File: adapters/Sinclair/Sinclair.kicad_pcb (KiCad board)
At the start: 2 copper layers, 22.9 x 18.4 mm, 2 parts, among them J1 JoyKEY, J2 Sinclair

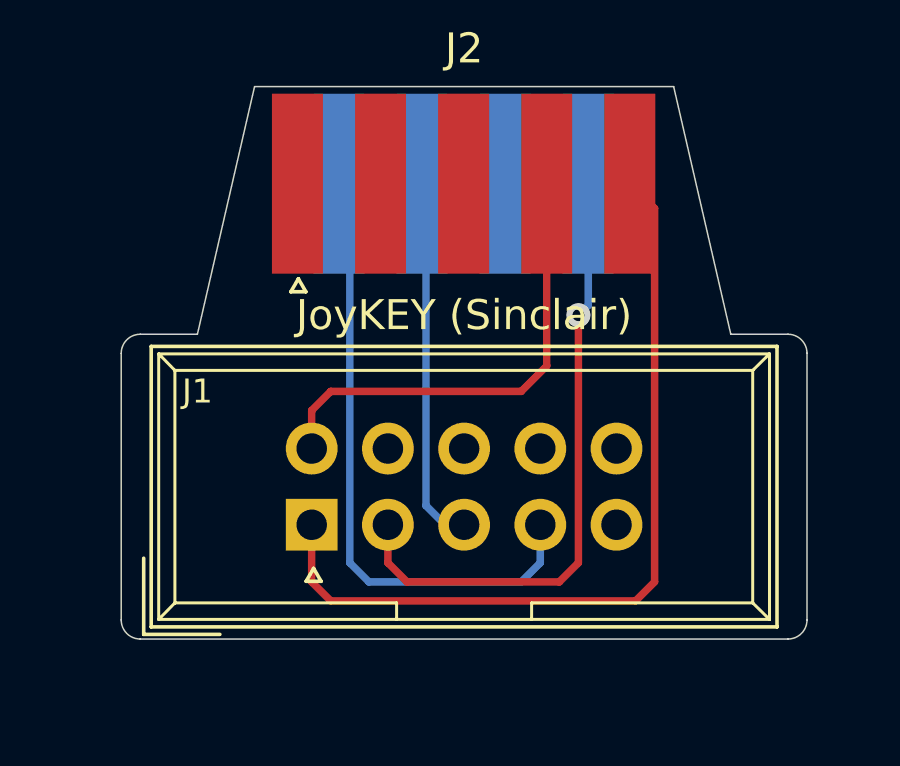
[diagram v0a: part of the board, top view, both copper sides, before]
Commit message: Fixed Sinclair adapter
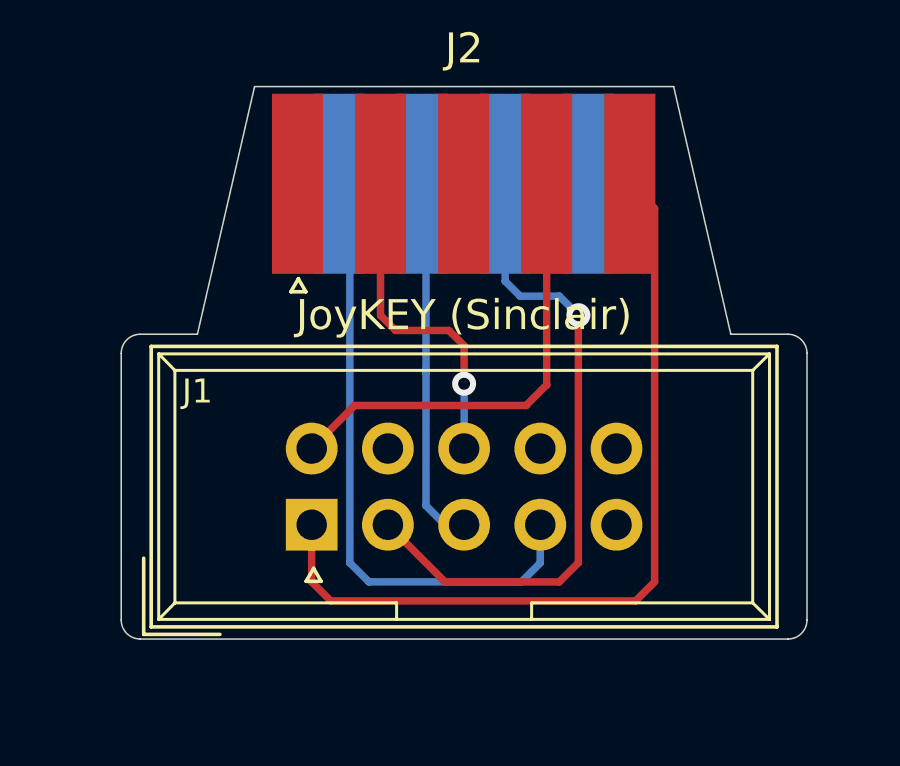
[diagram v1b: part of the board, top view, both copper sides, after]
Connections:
- J1 pad 10: Net-(J1-Pad10) -> (no net)
- J1 pad 5: Net-(J1-Pad5) -> (no net)
- J1 pad 7: Net-(J1-Pad7) -> (no net)
- J1 pad 9: Net-(J1-Pad9) -> (no net)
- J2 pad 1: Net-(J2-Pad1) -> (no net)
- J2 pad 2: Net-(J2-Pad2) -> GND
- J2 pad 3: Net-(J2-Pad3) -> (no net)
- J2 pad 8: GND -> /DOWN
- J2 pad 9: /DOWN -> (no net)
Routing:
- net GND: track 0.00 -> 11.0 mm, vias 0 -> 1
- net /DOWN: track 20.9 -> 21.8 mm

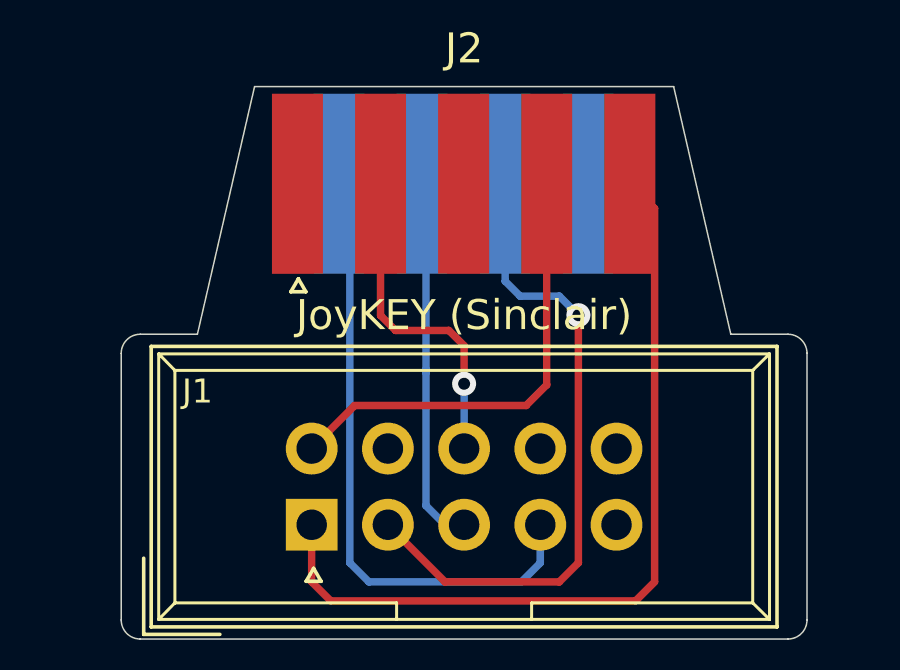
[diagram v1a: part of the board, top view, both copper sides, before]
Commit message: Tweaked sinclair adapter
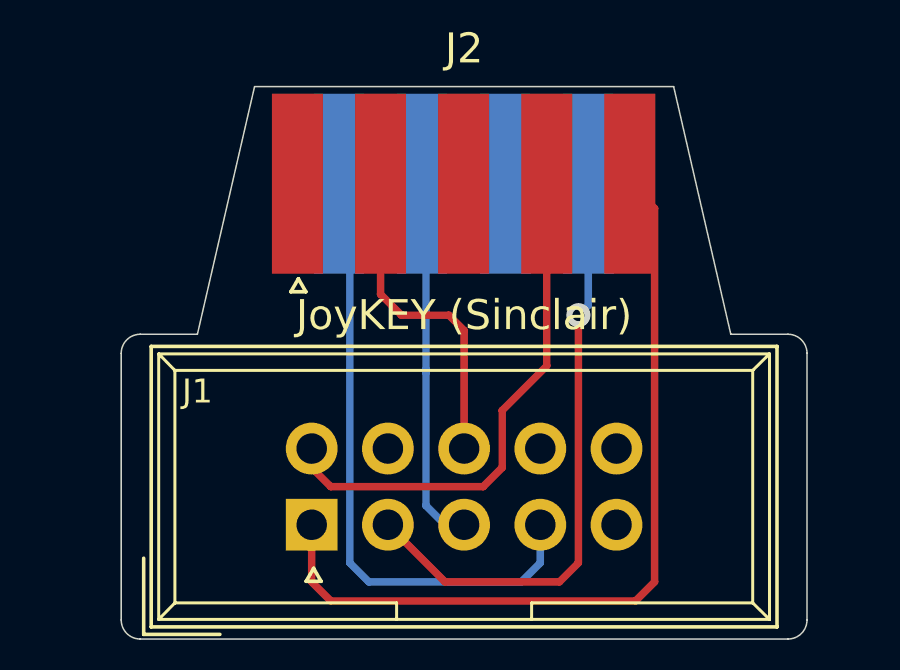
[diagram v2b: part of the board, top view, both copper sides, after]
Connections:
- J2 pad 8: /DOWN -> GND
- J2 pad 9: (no net) -> /DOWN
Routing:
- net /FIRE: track 15.4 -> 17.6 mm
- net /DOWN: track 21.8 -> 20.2 mm
- net GND: track 11.0 -> 10.9 mm, vias 1 -> 0
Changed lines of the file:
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@@
     (thickness 1.6)
     (drawings 16)
-    (tracks 38)
+    (tracks 37)
     (zones 0)
     (modules 2)
@@
       (net 4 /LEFT))
     (pad 8 smd rect (at 1.3695 0.0635 180) (size 1.7 6) (layers B.Cu B.Paste B.Mask)
+      (net 1 GND))
+    (pad 9 smd rect (at 4.1395 0.0635 180) (size 1.7 6) (layers B.Cu B.Paste B.Mask)
       (net 3 /DOWN))
-    (pad 9 smd rect (at 4.1395 0.0635 180) (size 1.7 6) (layers B.Cu B.Paste B.Mask))
     (pad 1 smd rect (at -5.5555 0.0635 180) (size 1.7 6) (layers F.Cu F.Paste F.Mask))
     (pad 2 smd rect (at -2.7855 0.0635 180) (size 1.7 6) (layers F.Cu F.Paste F.Mask)
@@
   (gr_line (start 130.81 92.71) (end 130.81 83.82) (layer Edge.Cuts) (width 0.05))
   (gr_line (start 153.035 93.345) (end 131.445 93.345) (layer Edge.Cuts) (width 0.05))
-  (via (at 142.24 84.836) (size 0.8) (drill 0.4) (layers F.Cu B.Cu) (net 1))
-  (segment (start 142.24 86.995) (end 142.24 84.836) (width 0.25) (layer B.Cu) (net 1))
-  (segment (start 142.24 83.566) (end 142.24 84.836) (width 0.25) (layer F.Cu) (net 1))
-  (segment (start 141.732 83.058) (end 142.24 83.566) (width 0.25) (layer F.Cu) (net 1))
-  (segment (start 139.954 83.058) (end 141.732 83.058) (width 0.25) (layer F.Cu) (net 1))
-  (segment (start 139.4545 82.5585) (end 139.954 83.058) (width 0.25) (layer F.Cu) (net 1))
-  (segment (start 139.4545 78.1685) (end 139.4545 82.5585) (width 0.25) (layer F.Cu) (net 1))
+  (segment (start 139.4545 78.1685) (end 139.4545 81.854185) (width 0.25) (layer F.Cu) (net 1) (status 10))
+  (segment (start 139.4545 81.854185) (end 140.150315 82.55) (width 0.25) (layer F.Cu) (net 1))
+  (segment (start 140.150315 82.55) (end 141.732008 82.55) (width 0.25) (layer F.Cu) (net 1))
+  (segment (start 142.24 83.057992) (end 141.732008 82.55) (width 0.25) (layer F.Cu) (net 1))
+  (segment (start 142.24 86.995) (end 142.24 83.057992) (width 0.25) (layer F.Cu) (net 1) (status 10))
   (segment (start 148.59 78.994) (end 147.7645 78.1685) (width 0.25) (layer F.Cu) (net 2) (status 30))
   (segment (start 148.59 91.44) (end 148.59 78.994) (width 0.25) (layer F.Cu) (net 2) (status 20))
@@
   (segment (start 137.16 89.535) (end 137.16 91.44) (width 0.25) (layer F.Cu) (net 2) (status 10))
   (via (at 146.05 82.550068) (size 0.8) (drill 0.4) (layers F.Cu B.Cu) (net 3))
-  (segment (start 139.7 89.535) (end 141.605 91.44) (width 0.25) (layer F.Cu) (net 3))
+  (segment (start 139.7 89.535) (end 141.605 91.44) (width 0.25) (layer F.Cu) (net 3) (status 10))
   (segment (start 141.605 91.44) (end 145.415 91.44) (width 0.25) (layer F.Cu) (net 3))
   (segment (start 145.415 91.44) (end 146.05 90.805) (width 0.25) (layer F.Cu) (net 3))
   (segment (start 146.05 90.805) (end 146.05 82.550068) (width 0.25) (layer F.Cu) (net 3))
-  (segment (start 144.106 81.915) (end 145.414932 81.915) (width 0.25) (layer B.Cu) (net 3))
-  (segment (start 145.414932 81.915) (end 146.05 82.550068) (width 0.25) (layer B.Cu) (net 3))
-  (segment (start 143.6095 81.4185) (end 144.106 81.915) (width 0.25) (layer B.Cu) (net 3))
-  (segment (start 143.6095 78.1685) (end 143.6095 81.4185) (width 0.25) (layer B.Cu) (net 3))
+  (segment (start 146.3795 82.220568) (end 146.05 82.550068) (width 0.25) (layer B.Cu) (net 3))
+  (segment (start 146.3795 78.1685) (end 146.3795 82.220568) (width 0.25) (layer B.Cu) (net 3) (status 10))
   (segment (start 141.605 89.535) (end 142.24 89.535) (width 0.25) (layer B.Cu) (net 4) (status 30))
   (segment (start 140.97 88.9) (end 141.605 89.535) (width 0.25) (layer B.Cu) (net 4) (status 20))
   (segment (start 140.97 84.455) (end 140.97 84.365) (width 0.25) (layer B.Cu) (net 4))
   (segment (start 140.97 84.455) (end 140.97 88.9) (width 0.25) (layer B.Cu) (net 4))
-  (segment (start 140.97 78.299) (end 140.8395 78.1685) (width 0.25) (layer B.Cu) (net 4))
-  (segment (start 140.97 84.455) (end 140.97 78.299) (width 0.25) (layer B.Cu) (net 4))
+  (segment (start 140.97 78.299) (end 140.8395 78.1685) (width 0.25) (layer B.Cu) (net 4) (status 30))
+  (segment (start 140.97 84.455) (end 140.97 78.299) (width 0.25) (layer B.Cu) (net 4) (status 20))
   (segment (start 144.78 90.805) (end 144.78 89.535) (width 0.25) (layer B.Cu) (net 5) (status 20))
   (segment (start 139.065 91.44) (end 144.145 91.44) (width 0.25) (layer B.Cu) (net 5))
@@
   (segment (start 144.145 91.44) (end 144.78 90.805) (width 0.25) (layer B.Cu) (net 5))
   (segment (start 138.0695 78.1685) (end 138.43 78.529) (width 0.25) (layer B.Cu) (net 5) (status 30))
-  (segment (start 144.308999 85.561001) (end 144.9945 84.8755) (width 0.25) (layer F.Cu) (net 6))
-  (segment (start 137.16 86.995) (end 138.593999 85.561001) (width 0.25) (layer F.Cu) (net 6))
-  (segment (start 138.593999 85.561001) (end 144.308999 85.561001) (width 0.25) (layer F.Cu) (net 6))
-  (segment (start 144.9945 84.8755) (end 144.9945 78.1685) (width 0.25) (layer F.Cu) (net 6))
+  (segment (start 144.9945 84.2405) (end 144.9945 78.1685) (width 0.25) (layer F.Cu) (net 6) (status 20))
+  (segment (start 143.51 87.63) (end 143.51 85.725) (width 0.25) (layer F.Cu) (net 6))
+  (segment (start 142.875 88.265) (end 143.51 87.63) (width 0.25) (layer F.Cu) (net 6))
+  (segment (start 137.795 88.265) (end 142.875 88.265) (width 0.25) (layer F.Cu) (net 6))
+  (segment (start 137.16 87.63) (end 137.795 88.265) (width 0.25) (layer F.Cu) (net 6) (status 10))
+  (segment (start 143.51 85.725) (end 144.9945 84.2405) (width 0.25) (layer F.Cu) (net 6))
+  (segment (start 137.16 86.995) (end 137.16 87.63) (width 0.25) (layer F.Cu) (net 6) (status 30))
   (zone (net 1) (net_name GND) (layer B.Cu) (hatch edge 0.508)
     (connect_pads (clearance 0.508))

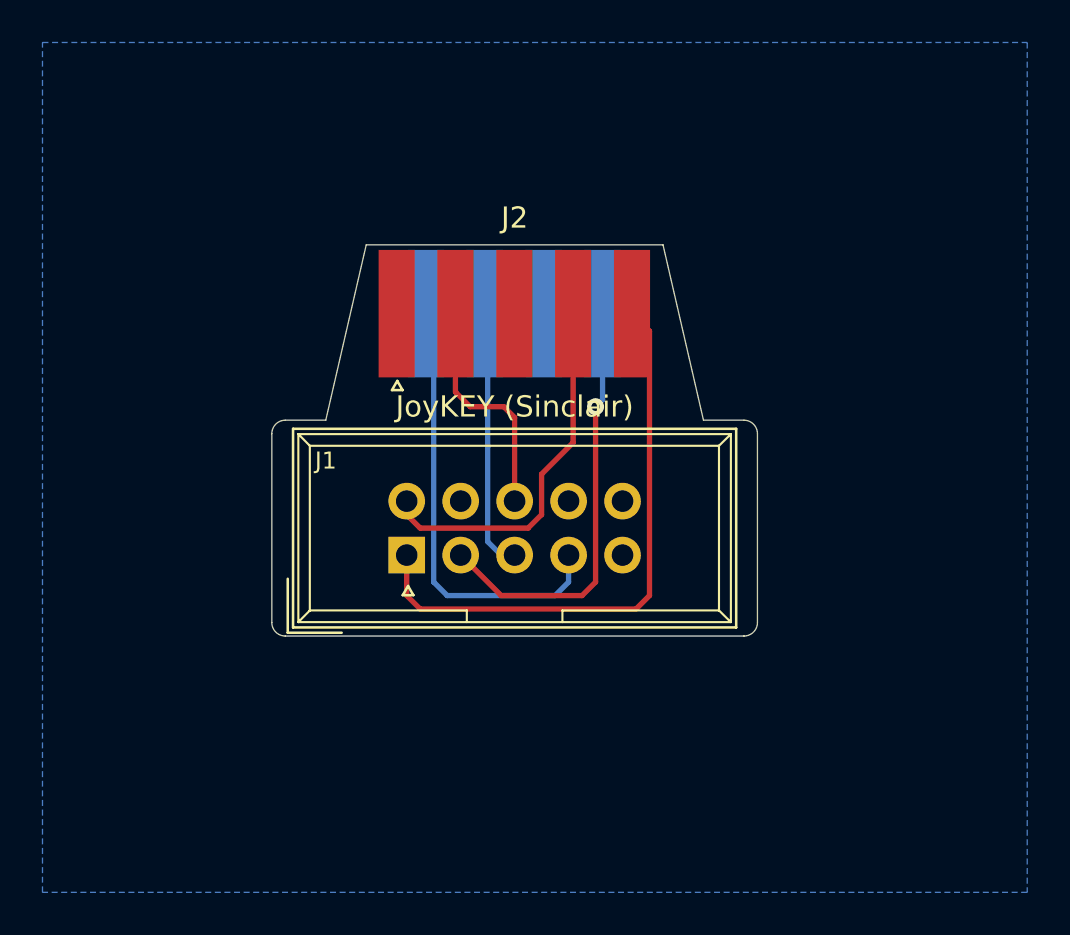
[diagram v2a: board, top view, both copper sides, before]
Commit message: Added male side to sinclair adapter
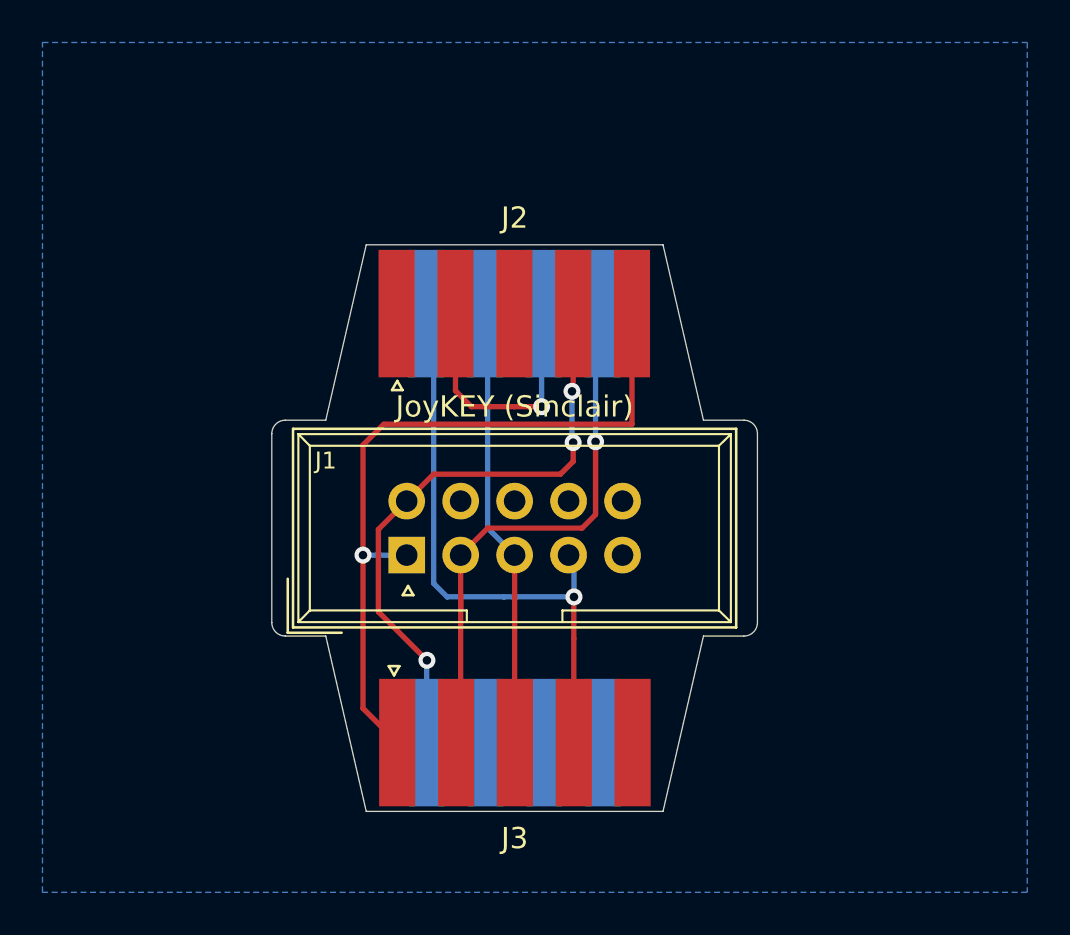
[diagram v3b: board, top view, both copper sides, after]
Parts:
- added J3: Atari, RND_DSUB:DSUB-9_Male_Edge, F.Cu at (142.2, 98.4)
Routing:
- net /FIRE: track 17.6 -> 28.5 mm, vias 0 -> 3
- net /LEFT: track 12.4 -> 20.8 mm
- net /UP: track 27.5 -> 35.2 mm, vias 0 -> 1
- net /RIGHT: track 20.9 -> 28.7 mm, vias 0 -> 1
- net /DOWN: track 20.2 -> 26.3 mm
- net GND: track 10.9 -> 12.4 mm, vias 0 -> 1
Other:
- board size 22.9 x 18.4 mm -> 22.9 x 26.7 mm
- board text added: "ATARI"
- board text added: "SINCLAIR"
